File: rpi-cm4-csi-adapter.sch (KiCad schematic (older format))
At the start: 19 parts, among them J1 687122149022, J2 WE_68715014522

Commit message: Generate local libraries
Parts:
- D1: footprint antmicro-footprints:LED_0603 -> rpi-cm4-csi-adapter-footprints:LED_0603; symbol antmicroLEDIndicationDiscrete:KP-1608CGCK -> rpi-cm4-csi-adapter:KP-1608CGCK
- J2: footprint antmicro-footprints:WE_68715014522 -> rpi-cm4-csi-adapter-footprints:WE_68715014522; symbol antmicroFCCConnectors:WE_68715014522 -> rpi-cm4-csi-adapter:WE_68715014522
- N1: footprint antmicro-footprints:antmicro-logo_scaled_12mm -> rpi-cm4-csi-adapter-footprints:antmicro-logo_scaled_12mm; symbol antmicroMechanicalParts:antmicro_logo -> rpi-cm4-csi-adapter:antmicro_logo
- N2: footprint antmicro-footprints:oshw-logo -> rpi-cm4-csi-adapter-footprints:oshw-logo; symbol antmicroMechanicalParts:oshw_logo -> rpi-cm4-csi-adapter:oshw_logo
- R1, R2: footprint antmicro-footprints:0402-res -> rpi-cm4-csi-adapter-footprints:0402-res; symbol antmicroResistors0402:R_0R_0402 -> rpi-cm4-csi-adapter:R_0R_0402
- R3: footprint antmicro-footprints:0402-res -> rpi-cm4-csi-adapter-footprints:0402-res; symbol antmicroResistors0402:R_330R_0402 -> rpi-cm4-csi-adapter:R_330R_0402
- TP1, TP2, TP3, TP4, TP5, TP6, TP7: footprint antmicro-footprints:TP-R-1.5 -> rpi-cm4-csi-adapter-footprints:TP-R-1.5; symbol antmicroTestPoints:TP -> rpi-cm4-csi-adapter:TP
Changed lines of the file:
@@
 NoConn ~ 9625 6200
 $Comp
-L antmicroMechanicalParts:antmicro_logo N1
+L rpi-cm4-csi-adapter:antmicro_logo N1
 U 1 1 620D8E74
 P 6575 10000
 F 0 "N1" H 6789 10093 50  0000 L CNN
 F 1 "antmicro_logo" H 6789 10002 50  0000 L CNN
-F 2 "antmicro-footprints:antmicro-logo_scaled_12mm" H 6475 10250 50  0001 C CNN
+F 2 "rpi-cm4-csi-adapter-footprints:antmicro-logo_scaled_12mm" H 6475 10250 50  0001 C CNN
 F 3 "" H 6575 10350 50  0001 C CNN
 	1    6575 10000
@@
 $EndComp
 $Comp
-L antmicroMechanicalParts:oshw_logo N2
+L rpi-cm4-csi-adapter:oshw_logo N2
 U 1 1 620D97AB
 P 6600 10200
 F 0 "N2" H 6794 10203 50  0000 L CNN
 F 1 "oshw_logo" H 6794 10112 50  0000 L CNN
-F 2 "antmicro-footprints:oshw-logo" H 6620 9960 50  0001 C CNN
+F 2 "rpi-cm4-csi-adapter-footprints:oshw-logo" H 6620 9960 50  0001 C CNN
 F 3 "" H 6600 10200 50  0001 C CNN
 	1    6600 10200
@@
 MIPI0_D3_N
 $Comp
-L antmicroFCCConnectors:WE_68715014522 J2
+L rpi-cm4-csi-adapter:WE_68715014522 J2
 U 1 1 620C5002
 P 9825 4600
 F 0 "J2" H 9905 3792 50  0000 L CNN
 F 1 "WE_68715014522" H 9905 3701 50  0000 L CNN
-F 2 "antmicro-footprints:WE_68715014522" H 9625 1050 50  0001 C CNN
+F 2 "rpi-cm4-csi-adapter-footprints:WE_68715014522" H 9625 1050 50  0001 C CNN
 F 3 "https://katalog.we-online.de/em/datasheet/6871xx14522.pdf" H 9825 950 50  0001 C CNN
 F 4 "68715014522 " H 10225 4000 60  0001 L CNN "MPN"
@@
 CAM1_D3_P
 $Comp
-L antmicroTestPoints:TP TP1
+L rpi-cm4-csi-adapter:TP TP1
 U 1 1 620C5B77
 P 7575 6800
 F 0 "TP1" V 7575 6700 50  0000 C CNN
 F 1 "TP" H 7575 6800 50  0001 C CNN
-F 2 "antmicro-footprints:TP-R-1.5" H 7575 6800 50  0001 C CNN
+F 2 "rpi-cm4-csi-adapter-footprints:TP-R-1.5" H 7575 6800 50  0001 C CNN
 F 3 "" H 7575 6800 50  0001 C CNN
 	1    7575 6800
@@
 $EndComp
 $Comp
-L antmicroTestPoints:TP TP2
+L rpi-cm4-csi-adapter:TP TP2
 U 1 1 620C6DC6
 P 7575 6900
 F 0 "TP2" V 7575 6800 50  0000 C CNN
 F 1 "TP" H 7575 6900 50  0001 C CNN
-F 2 "antmicro-footprints:TP-R-1.5" H 7575 6900 50  0001 C CNN
+F 2 "rpi-cm4-csi-adapter-footprints:TP-R-1.5" H 7575 6900 50  0001 C CNN
 F 3 "" H 7575 6900 50  0001 C CNN
 	1    7575 6900
@@
 $EndComp
 $Comp
-L antmicroTestPoints:TP TP3
+L rpi-cm4-csi-adapter:TP TP3
 U 1 1 620C7722
 P 8725 7000
 F 0 "TP3" V 8725 6900 50  0000 C CNN
 F 1 "TP" H 8725 7000 50  0001 C CNN
-F 2 "antmicro-footprints:TP-R-1.5" H 8725 7000 50  0001 C CNN
+F 2 "rpi-cm4-csi-adapter-footprints:TP-R-1.5" H 8725 7000 50  0001 C CNN
 F 3 "" H 8725 7000 50  0001 C CNN
 	1    8725 7000
@@
 $EndComp
 $Comp
-L antmicroTestPoints:TP TP4
+L rpi-cm4-csi-adapter:TP TP4
 U 1 1 620C7B7D
 P 8725 7100
 F 0 "TP4" V 8725 7000 50  0000 C CNN
 F 1 "TP" H 8725 7100 50  0001 C CNN
-F 2 "antmicro-footprints:TP-R-1.5" H 8725 7100 50  0001 C CNN
+F 2 "rpi-cm4-csi-adapter-footprints:TP-R-1.5" H 8725 7100 50  0001 C CNN
 F 3 "" H 8725 7100 50  0001 C CNN
 	1    8725 7100
@@
 $EndComp
 $Comp
-L antmicroResistors0402:R_0R_0402 R1
+L rpi-cm4-csi-adapter:R_0R_0402 R1
 U 1 1 620C8651
 P 8400 6800
 F 0 "R1" H 8200 6850 60  0000 C CNN
 F 1 "R_0R_0402" H 8400 6650 60  0001 C CNN
-F 2 "antmicro-footprints:0402-res" H 8600 7000 60  0001 L CNN
+F 2 "rpi-cm4-csi-adapter-footprints:0402-res" H 8600 7000 60  0001 L CNN
 F 3 "" H 8400 6800 50  0001 C CNN
 F 4 "PANASONIC" H 8600 7200 60  0001 L CNN "Manufacturer"
@@
 $EndComp
 $Comp
-L antmicroResistors0402:R_0R_0402 R2
+L rpi-cm4-csi-adapter:R_0R_0402 R2
 U 1 1 620C8C50
 P 8400 6900
 F 0 "R2" H 8200 6825 60  0000 C CNN
 F 1 "R_0R_0402" H 8400 6750 60  0001 C CNN
-F 2 "antmicro-footprints:0402-res" H 8600 7100 60  0001 L CNN
+F 2 "rpi-cm4-csi-adapter-footprints:0402-res" H 8600 7100 60  0001 L CNN
 F 3 "" H 8400 6900 50  0001 C CNN
 F 4 "PANASONIC" H 8600 7300 60  0001 L CNN "Manufacturer"
@@
 $EndComp
 $Comp
-L antmicroTestPoints:TP TP6
+L rpi-cm4-csi-adapter:TP TP6
 U 1 1 620EC6D1
 P 8950 7500
 F 0 "TP6" V 8950 7400 50  0000 C CNN
 F 1 "TP" H 8950 7500 50  0001 C CNN
-F 2 "antmicro-footprints:TP-R-1.5" H 8950 7500 50  0001 C CNN
+F 2 "rpi-cm4-csi-adapter-footprints:TP-R-1.5" H 8950 7500 50  0001 C CNN
 F 3 "" H 8950 7500 50  0001 C CNN
 	1    8950 7500
@@
 	8950 7600 9375 7600
 $Comp
-L antmicroTestPoints:TP TP5
+L rpi-cm4-csi-adapter:TP TP5
 U 1 1 620ED0C0
 P 8850 7800
 F 0 "TP5" V 8850 7700 50  0000 C CNN
 F 1 "TP" H 8850 7800 50  0001 C CNN
-F 2 "antmicro-footprints:TP-R-1.5" H 8850 7800 50  0001 C CNN
+F 2 "rpi-cm4-csi-adapter-footprints:TP-R-1.5" H 8850 7800 50  0001 C CNN
 F 3 "" H 8850 7800 50  0001 C CNN
 	1    8850 7800
@@
 VCC_3V3
 $Comp
-L antmicroLEDIndicationDiscrete:KP-1608CGCK D1
+L rpi-cm4-csi-adapter:KP-1608CGCK D1
 U 1 1 620F57C7
 P 7325 7825
 F 0 "D1" H 6675 8125 60  0000 C CNN
 F 1 "KP-1608CGCK" H 6950 8025 60  0000 C CNN
-F 2 "antmicro-footprints:LED_0603" H 7525 8025 60  0001 L CNN
+F 2 "rpi-cm4-csi-adapter-footprints:LED_0603" H 7525 8025 60  0001 L CNN
 F 3 "http://www.farnell.com/datasheets/2045956.pdf" H 7525 8125 60  0001 L CNN
 F 4 "KP-1608CGCK" H 7525 8325 60  0001 L CNN "MPN"
@@
 $EndComp
 $Comp
-L antmicroResistors0402:R_330R_0402 R3
+L rpi-cm4-csi-adapter:R_330R_0402 R3
 U 1 1 620F6AB5
 P 7575 7825
 F 0 "R3" H 7575 8038 60  0000 C CNN
 F 1 "R_330R_0402" H 7575 7675 60  0001 C CNN
-F 2 "antmicro-footprints:0402-res" H 7775 8025 60  0001 L CNN
+F 2 "rpi-cm4-csi-adapter-footprints:0402-res" H 7775 8025 60  0001 L CNN
 F 3 "" H 7575 7825 50  0001 C CNN
 F 4 "MULTICOMP" H 7775 8225 60  0001 L CNN "Manufacturer"
@@
 	7850 7825 7850 7950
 $Comp
-L antmicroTestPoints:TP TP7
+L rpi-cm4-csi-adapter:TP TP7
 U 1 1 6210E036
 P 5950 4700
 F 0 "TP7" V 5950 4600 50  0000 C CNN
 F 1 "TP" H 5950 4700 50  0001 C CNN
-F 2 "antmicro-footprints:TP-R-1.5" H 5950 4700 50  0001 C CNN
+F 2 "rpi-cm4-csi-adapter-footprints:TP-R-1.5" H 5950 4700 50  0001 C CNN
 F 3 "" H 5950 4700 50  0001 C CNN
 	1    5950 4700

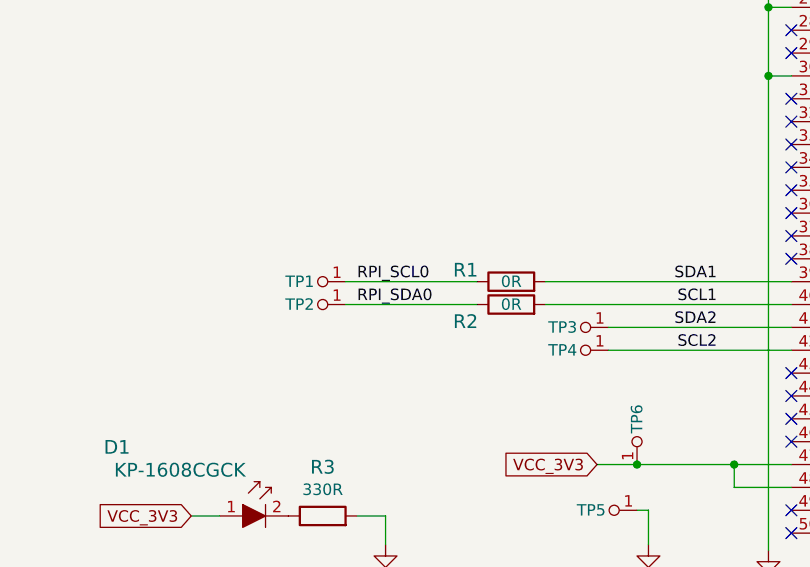
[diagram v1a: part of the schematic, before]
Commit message: Swap I2C lines - bump revision to 1.0.1
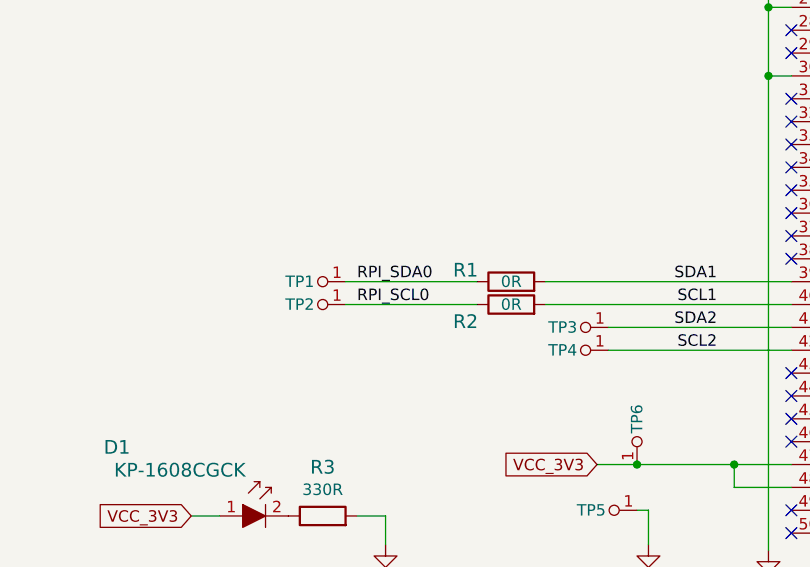
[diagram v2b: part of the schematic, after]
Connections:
- net RPI_SCL0: now also R2.1, TP2.1; no longer R1.1, TP1.1
- net RPI_SDA0: now also R1.1, TP1.1; no longer R2.1, TP2.1
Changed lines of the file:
@@
 Sheet 1 1
 Title "RPi CM4 CSI adapter"
-Date "2022-02-16"
-Rev "1.0.0"
+Date "2022-04"
+Rev "1.0.1"
 Comp ""
 Comment1 "www.antmicro.com"
@@
 	-1   0    0    -1
 $EndComp
+Text Label 7725 6900 0    50   ~ 0
+RPI_SCL0
 Text Label 7725 6800 0    50   ~ 0
-RPI_SCL0
-Text Label 7725 6900 0    50   ~ 0
 RPI_SDA0
 Wire Wire Line
